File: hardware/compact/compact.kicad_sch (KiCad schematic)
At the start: 13 parts, among them U3 RP2350A-QFN60

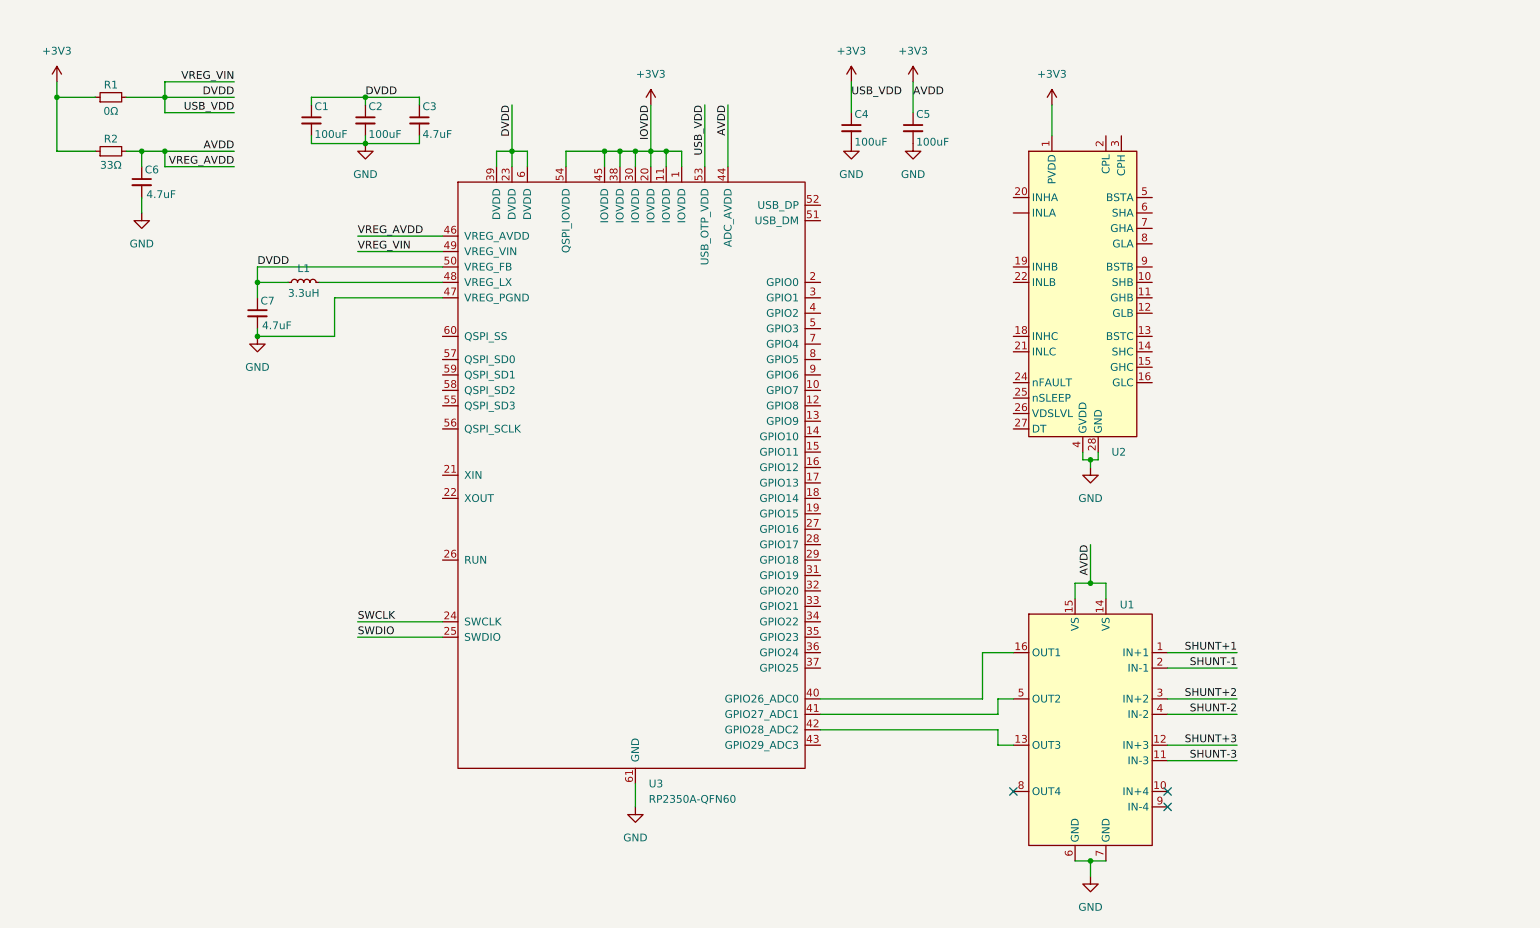
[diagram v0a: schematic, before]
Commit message: [Compact] Adding in the front-end FETS and USB
Signed-off-by: Greg Balke <gbalke@berkeley.edu>
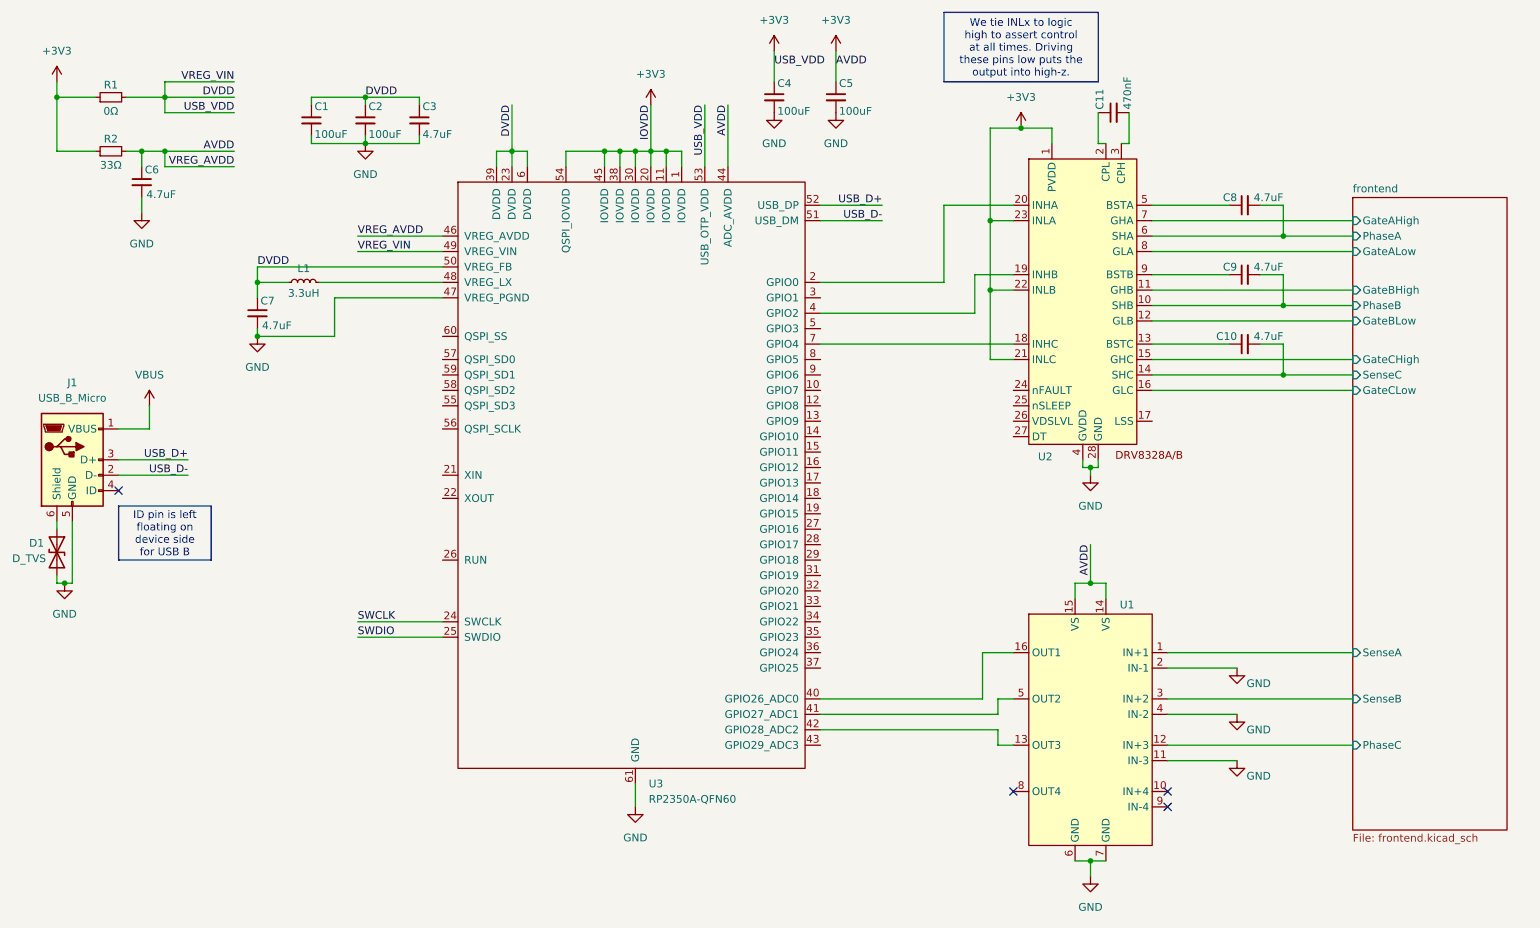
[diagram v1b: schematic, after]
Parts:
- added C10, C8, C9: 4.7uF, symbol Device:C_Small
- added C11: 470nF, symbol Device:C_Small
- added D1: D_TVS, symbol Device:D_TVS
- added J1: USB_B_Micro, symbol Connector:USB_B_Micro
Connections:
- net SHUNT-1 is gone; now on net GND: U1.2 (IN-1)
- net SHUNT-2 is gone; now on net GND: U1.4 (IN-2)
- net SHUNT-3 is gone; now on net GND: U1.11 (IN-3)
- net +3V3: now also U2.21 (INLC), U2.22 (INLB), U2.23 (INLA)
- net GND: now also D1.2 (A2), J1.5 (GND)
- net at U3.2 (GPIO0): now also U2.20 (INHA)
- net at U3.4 (GPIO2): now also U2.19 (INHB)
- net USB_D-: now reaches U3.51 (USB_DM)
- net USB_D-: now also J1.2 (D-)
- net USB_D+: now reaches U3.52 (USB_DP)
- net USB_D+: now also J1.3 (D+)
- net at U3.7 (GPIO4): now also U2.18 (INHC)
- net frontend/PhaseB: now reaches U2.10 (SHB)
- net frontend/PhaseB: now also C9.2
- net frontend/GateBHigh: now reaches U2.11 (GHB)
- net frontend/GateBLow: now reaches U2.12 (GLB)
- net at U2.13 (BSTC): now also C10.1
- net frontend/SenseC: now reaches U2.14 (SHC)
- net frontend/SenseC: now also C10.2
- net frontend/GateCHigh: now reaches U2.15 (GHC)
- net frontend/GateCLow: now reaches U2.16 (GLC)
- net at U2.2 (CPL): now also C11.1
- net at U2.3 (CPH): now also C11.2
- net at U2.5 (BSTA): now also C8.1
- net frontend/PhaseA: now reaches U2.6 (SHA)
- net frontend/PhaseA: now also C8.2
- net frontend/GateAHigh: now reaches U2.7 (GHA)
- net frontend/GateALow: now reaches U2.8 (GLA)
- net at U2.9 (BSTB): now also C9.1
- net SHUNT+1 renamed frontend/SenseA
- net SHUNT+2 renamed frontend/SenseB
- net SHUNT+3 renamed frontend/PhaseC
- new net: D1.1 (A1), J1.6 (Shield)
- new net VBUS: J1.1 (VBUS)
- no-connect marks 3 -> 4
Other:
- added sheet frontend (frontend.kicad_sch)
- moved on the sheet: C4, C5
